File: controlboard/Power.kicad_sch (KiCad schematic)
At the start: 20 parts, among them J11 Pololu Voltage Regulator, J12 USB_C_Receptacle_USB2.0_14P, Q2 PMOS-TODO, U3 AMS1117-3.3, U4 CH224K

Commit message: Control Board major progress
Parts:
- added J15: Jack-DC, symbol Connector:Jack-DC
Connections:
- net GND: now also J15.2
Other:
- note added: "REVERSE PROTECTION"
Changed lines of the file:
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@@
+		)
+	)
+	(text "REVERSE PROTECTION"
+		(exclude_from_sim no)
+		(at 204.724 69.342 0)
+		(effects
+			(font
+				(size 1.27 1.27)
+			)
 		)
 	)
@@
 		)
 	)
+	(hierarchical_label "MotorVoltage"
+		(shape input)
+		(at 207.01 63.5 0)
+		(fields_autoplaced yes)
+		(effects
+			(font
+				(size 1.27 1.27)
+			)
+			(justify left)
+		)
+	)
 	(hierarchical_label "5V"
 		(shape input)
@@
 	(symbol
 		(lib_id "power:GND")
+		(at 191.77 68.58 0)
+		(unit 1)
+		(exclude_from_sim no)
+		(in_bom yes)
+		(on_board yes)
+		(dnp no)
+		(fields_autoplaced yes)
+		(property "Reference" "#PWR09"
+			(at 191.77 74.93 0)
+			(effects
+				(font
+					(size 1.27 1.27)
+				)
+				(hide yes)
+			)
+		)
+		(property "Value" "GND"
+			(at 191.77 73.66 0)
+			(effects
+				(font
+					(size 1.27 1.27)
+				)
+				(hide yes)
+			)
+		)
+		(property "Footprint" ""
+			(at 191.77 68.58 0)
+			(effects
+				(font
+					(size 1.27 1.27)
+				)
+				(hide yes)
+			)
+		)
+		(property "Datasheet" ""
+			(at 191.77 68.58 0)
+			(effects
+				(font
+					(size 1.27 1.27)
+				)
+				(hide yes)
+			)
+		)
+		(property "Description" "Power symbol creates a global label with name \"GND\" , ground"
+			(at 191.77 68.58 0)
+			(effects
+				(font
+					(size 1.27 1.27)
+				)
+				(hide yes)
+			)
+		)
+		(pin "1"
+		)
+		(instances
+			(project "controlboard"
+				(path "/2797250d-6fee-4769-b4dd-0e20ce4f0941/5fab4b81-761e-4fae-b113-00364a75fd9a"
+					(reference "#PWR09")
+					(unit 1)
+				)
+			)
+		)
+	)
+	(symbol
+		(lib_id "power:GND")
 		(at 77.47 43.18 0)
 		(unit 1)
@@
 					(unit 1)
 				)
+			)
+		)
+	)
+	(symbol
+		(lib_id "Connector:Jack-DC")
+		(at 184.15 66.04 0)
+		(unit 1)
+		(exclude_from_sim no)
+		(in_bom yes)
+		(on_board yes)
+		(dnp no)
+		(fields_autoplaced yes)
+		(property "Reference" "J15"
+			(at 184.15 57.15 0)
+			(effects
+				(font
+					(size 1.27 1.27)
+				)
+			)
+		)
+		(property "Value" "Jack-DC"
+			(at 184.15 59.69 0)
+			(effects
+				(font
+					(size 1.27 1.27)
+				)
+			)
+		)
+		(property "Footprint" ""
+			(at 185.42 67.056 0)
+			(effects
+				(font
+					(size 1.27 1.27)
+				)
+				(hide yes)
+			)
+		)
+		(property "Datasheet" "~"
+			(at 185.42 67.056 0)
+			(effects
+				(font
+					(size 1.27 1.27)
+				)
+				(hide yes)
+			)
+		)
+		(property "Description" "DC Barrel Jack"
+			(at 184.15 66.04 0)
+			(effects
+				(font
+					(size 1.27 1.27)
+				)
+				(hide yes)
+			)
+		)
+		(pin "2"
+		)
+		(pin "1"
+		)
+		(instances
+			(project "controlboard"
+				(path "/2797250d-6fee-4769-b4dd-0e20ce4f0941/5fab4b81-761e-4fae-b113-00364a75fd9a"
+					(reference "J15")
+					(unit 1)
+				)

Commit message: more progress on controlboard pcb
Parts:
- removed D2: LED, symbol Device:LED
- removed R2: 1k, symbol Device:R
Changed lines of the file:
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@@
-	)
-	(junction
-		(at 140.97 39.37)
-		(diameter 0)
-		(color 0 0 0 0)
 	)
 	(junction
@@
 	(wire
 		(pts
-			(xy 140.97 39.37) (xy 138.43 39.37)
+			(xy 138.43 39.37) (xy 142.24 39.37)
 		)
 		(stroke
@@
 	(wire
 		(pts
-			(xy 140.97 39.37) (xy 148.59 39.37)
-		)
-		(stroke
-			(width 0)
-			(type default)
-		)
-	)
-	(wire
-		(pts
 			(xy 78.74 49.53) (xy 68.58 49.53)
 		)
@@
 		(pts
 			(xy 113.03 52.07) (xy 120.65 52.07)
-		)
-		(stroke
-			(width 0)
-			(type default)
-		)
-	)
-	(wire
-		(pts
-			(xy 140.97 48.26) (xy 140.97 46.99)
 		)
 		(stroke
@@
 	(hierarchical_label "MotorVoltage"
 		(shape input)
-		(at 148.59 39.37 0)
+		(at 142.24 39.37 0)
 		(fields_autoplaced yes)
 		(effects
@@
 	)
 	(symbol
-		(lib_id "Device:R")
-		(at 140.97 52.07 0)
-		(mirror x)
-		(unit 1)
-		(exclude_from_sim no)
-		(in_bom yes)
-		(on_board yes)
-		(dnp no)
-		(property "Reference" "R2"
-			(at 147.32 52.07 90)
-			(effects
-				(font
-					(size 1.27 1.27)
-				)
-			)
-		)
-		(property "Value" "1k"
-			(at 144.78 52.07 90)
-			(effects
-				(font
-					(size 1.27 1.27)
-				)
-			)
-		)
-		(property "Footprint" ""
-			(at 139.192 52.07 90)
-			(effects
-				(font
-					(size 1.27 1.27)
-				)
-				(hide yes)
-			)
-		)
-		(property "Datasheet" "~"
-			(at 140.97 52.07 0)
-			(effects
-				(font
-					(size 1.27 1.27)
-				)
-				(hide yes)
-			)
-		)
-		(property "Description" "Resistor"
-			(at 140.97 52.07 0)
-			(effects
-				(font
-					(size 1.27 1.27)
-				)
-				(hide yes)
-			)
-		)
-		(pin "2"
-		)
-		(pin "1"
-		)
-		(instances
-			(project "controlboard"
-				(path "/2797250d-6fee-4769-b4dd-0e20ce4f0941/5fab4b81-761e-4fae-b113-00364a75fd9a"
-					(reference "R2")
-					(unit 1)
-				)
-			)
-		)
-	)
-	(symbol
 		(lib_id "Device:C")
 		(at 259.08 92.71 0)
@@
 					(unit 1)
 				)
-			)
-		)
-	)
-	(symbol
-		(lib_id "power:GND")
-		(at 140.97 55.88 0)
-		(unit 1)
-		(exclude_from_sim no)
-		(in_bom yes)
-		(on_board yes)
-		(dnp no)
-		(fields_autoplaced yes)
-		(property "Reference" "#PWR017"
-			(at 140.97 62.23 0)
-			(effects
-				(font
-					(size 1.27 1.27)
-				)
-				(hide yes)
-			)
-		)
-		(property "Value" "GND"
-			(at 140.97 60.96 0)
-			(effects
-				(font
-					(size 1.27 1.27)
-				)
-				(hide yes)
-			)
-		)
-		(property "Footprint" ""
-			(at 140.97 55.88 0)
-			(effects
-				(font
-					(size 1.27 1.27)
-				)
-				(hide yes)
-			)
-		)
-		(property "Datasheet" ""
-			(at 140.97 55.88 0)
-			(effects
-				(font
-					(size 1.27 1.27)
-				)
-				(hide yes)
-			)
-		)
-		(property "Description" "Power symbol creates a global label with name \"GND\" , ground"
-			(at 140.97 55.88 0)
-			(effects
-				(font
-					(size 1.27 1.27)
-				)
-				(hide yes)
-			)
-		)
-		(pin "1"
-		)
-		(instances
-			(project "controlboard"
-				(path "/2797250d-6fee-4769-b4dd-0e20ce4f0941/5fab4b81-761e-4fae-b113-00364a75fd9a"
-					(reference "#PWR017")
-					(unit 1)
-				)
-			)
-		)
-	)
-	(symbol
-		(lib_id "Device:LED")
-		(at 140.97 43.18 270)
-		(mirror x)
-		(unit 1)
-		(exclude_from_sim no)
-		(in_bom yes)
-		(on_board yes)
-		(dnp no)
-		(property "Reference" "D2"
-			(at 147.32 44.7675 0)
-			(effects
-				(font
-					(size 1.27 1.27)
-				)
-			)
-		)
-		(property "Value" "LED"
-			(at 144.78 44.7675 0)
-			(effects
-				(font
-					(size 1.27 1.27)
-				)
-			)
-		)
-		(property "Footprint" ""
-			(at 140.97 43.18 0)
-			(effects
-				(font
-					(size 1.27 1.27)
-				)
-				(hide yes)
-			)
-		)
-		(property "Datasheet" "~"
-			(at 140.97 43.18 0)
-			(effects
-				(font
-					(size 1.27 1.27)
-				)
-				(hide yes)
-			)
-		)
-		(property "Description" "Light emitting diode"
-			(at 140.97 43.18 0)
-			(effects
-				(font
-					(size 1.27 1.27)
-				)
-				(hide yes)
-			)
-		)
-		(pin "1"
-		)
-		(pin "2"
-		)
-		(instances
-			(project "controlboard"
-				(path "/2797250d-6fee-4769-b4dd-0e20ce4f0941/5fab4b81-761e-4fae-b113-00364a75fd9a"
-					(reference "D2")
-					(unit 1)
-				)

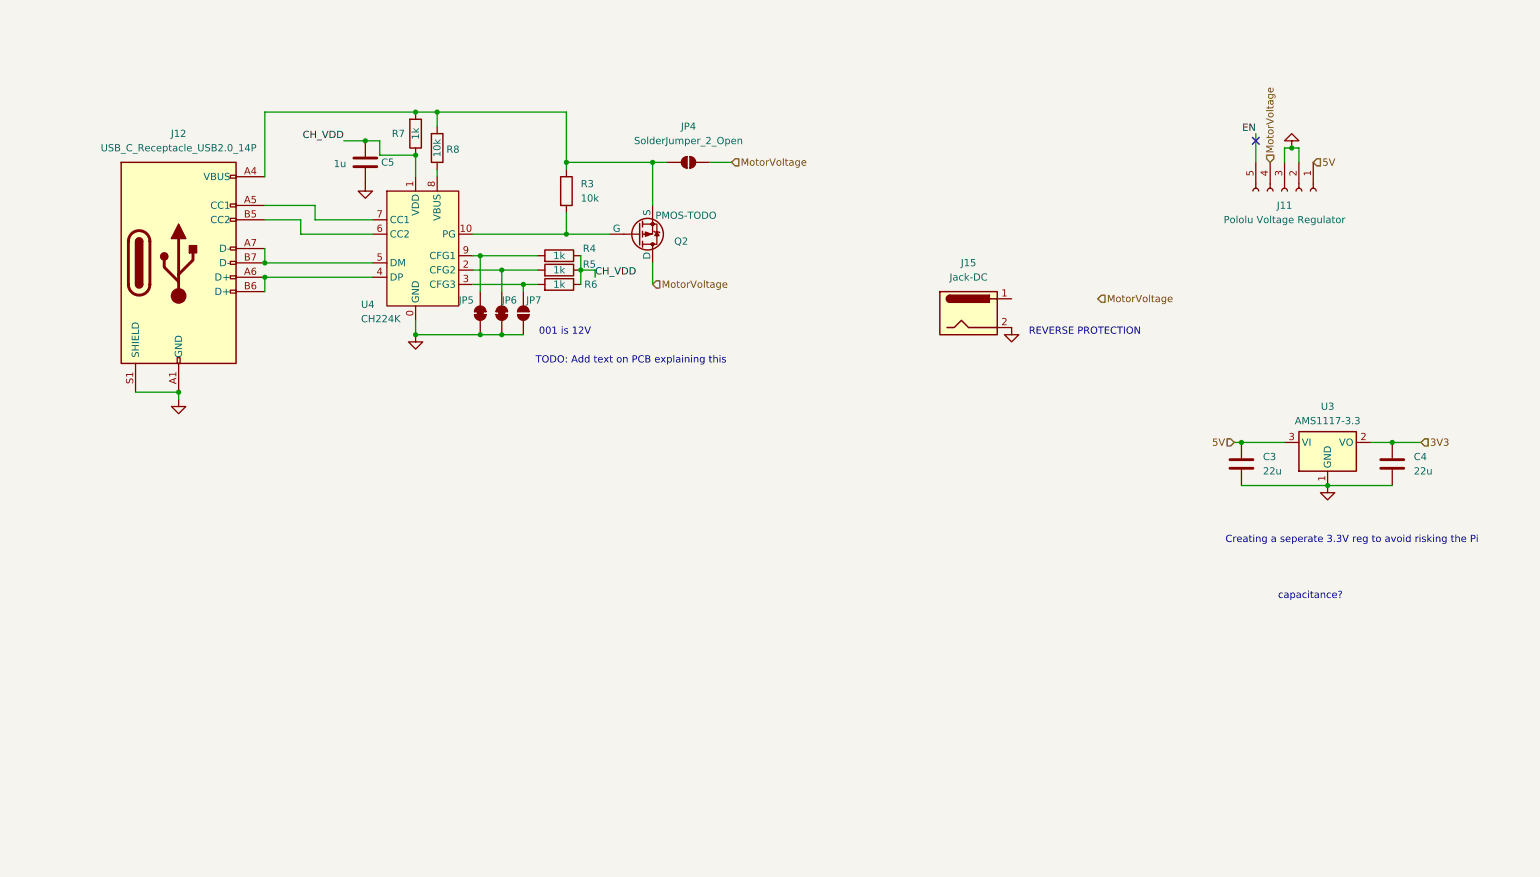
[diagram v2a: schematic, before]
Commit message: ControlBoard Schematic nearly done
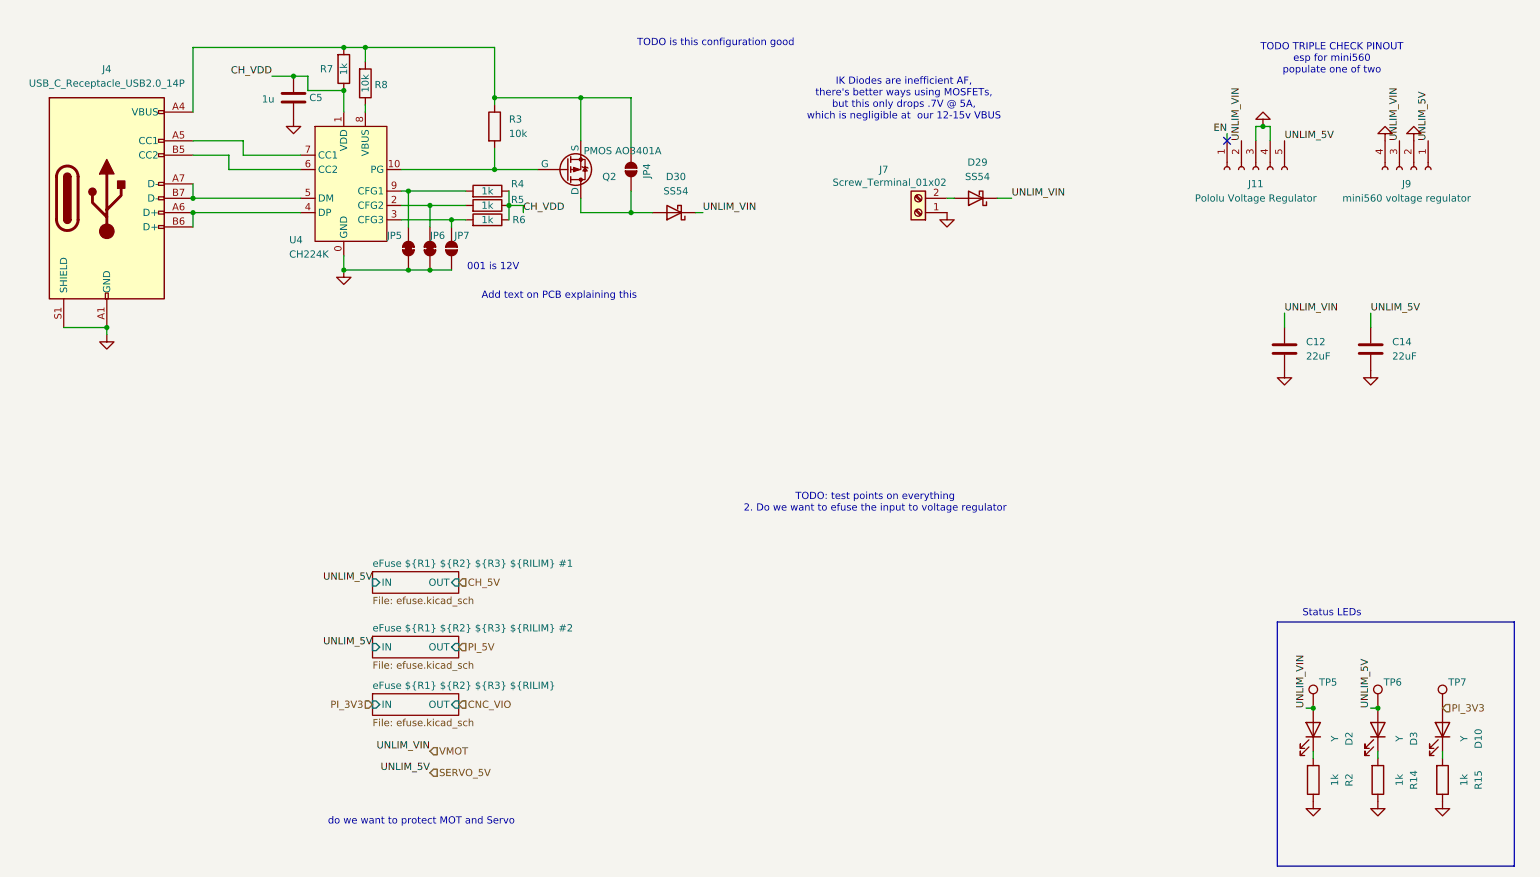
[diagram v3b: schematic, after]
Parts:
- removed C3, C4: 22u, symbol Device:C
- removed J15: Jack-DC, symbol Connector:Jack-DC
- removed U3: AMS1117-3.3, Package_TO_SOT_SMD:SOT-223-3_TabPin2, symbol Regulator_Linear:AMS1117-3.3
- added C12, C14: 22uF, Capacitor_SMD:C_1206_3216Metric_Pad1.33x1.80mm_HandSolder, symbol Device:C
- added D10, D2, D3: Y, LED_SMD:LED_0603_1608Metric_Pad1.05x0.95mm_HandSolder, symbol Device:LED
- added D29, D30: SS54, Diode_SMD:D_SMA_Handsoldering, symbol Device:D_Schottky
- added J7: Screw_Terminal_01x02, TerminalBlock_RND:TerminalBlock_RND_205-00287_1x02_P5.08mm_Horizontal, symbol Connector:Screw_Terminal_01x02
- added J9: mini560 voltage regulator, 0chessbot-parts:mini560, symbol Connector:Conn_01x04_Socket
- added R14, R15, R2: 1k, Resistor_SMD:R_0603_1608Metric_Pad0.98x0.95mm_HandSolder, symbol Device:R
- added TP5, TP6, TP7: TestPoint, Connector_PinSocket_2.54mm:PinSocket_1x01_P2.54mm_Vertical, symbol Connector:TestPoint
- C5: footprint (none) -> Capacitor_SMD:C_0603_1608Metric_Pad1.08x0.95mm_HandSolder
- J11: footprint (none) -> 0chessbot-parts:reg15d
- J4: renamed from J12; footprint (none) -> Connector_USB:USB_C_Receptacle_HRO_TYPE-C-31-M-12
- JP4, JP7: footprint (none) -> Jumper:SolderJumper-2_P1.3mm_Open_RoundedPad1.0x1.5mm
- JP5, JP6: footprint (none) -> Jumper:SolderJumper-2_P1.3mm_Bridged2Bar_RoundedPad1.0x1.5mm
- Q2: value PMOS-TODO -> PMOS AO3401A; footprint (none) -> Package_TO_SOT_SMD:SOT-23_Handsoldering
- R3, R4, R5, R6, R7, R8: footprint (none) -> Resistor_SMD:R_0603_1608Metric_Pad0.98x0.95mm_HandSolder
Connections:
- net 5V is gone; now on net EN: J11.1 (Pin_1)
- net EN: no longer J11.5 (Pin_5)
- net GND: now also J11.4 (Pin_4), C12.2, C14.2, J7.1 (Pin_1), J9.2 (Pin_2), J9.4 (Pin_4), R14.1, R15.1, R2.1; no longer J11.2 (Pin_2)
- net MotorVoltage: no longer names the net of JP4.2 (B), Q2.1 (D)
- net MotorVoltage: now also D30.2 (A); no longer J11.4 (Pin_4)
- new net: D10.1 (K), R15.2
- new net: D29.2 (A), J7.2 (Pin_2)
- new net: D3.1 (K), R14.2
- new net: D2.1 (K), R2.2
- new net PI_3V3: D10.2 (A), TP7.1
- new net SERVO_5V: C14.1, D3.2 (A), J11.5 (Pin_5), J9.1 (Pin_1), TP6.1
- new net VMOT: C12.1, D2.2 (A), D29.1 (K), D30.1 (K), J11.2 (Pin_2), J9.3 (Pin_3), TP5.1
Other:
- added sheet eFuse ${R1} ${R2} ${R3} ${RILIM} (efuse.kicad_sch)
- added sheet eFuse ${R1} ${R2} ${R3} ${RILIM} #1 (efuse.kicad_sch)
- added sheet eFuse ${R1} ${R2} ${R3} ${RILIM} #2 (efuse.kicad_sch)
- note added: "Add text on PCB explaining this"
- note added: "IK Diodes are inefficient AF, there's better ways using MOSFETs, but this only drops .7V @ 5A, which is negligible at our 12-15v VBUS"
- note added: "Status LEDs"
- note added: "TODO TRIPLE CHECK PINOUT esp for mini560 populate one of two"
- note added: "TODO is this configuration good"
- note added: "TODO: test points on everything 2. Do we want to efuse the input to voltage regulator"
- note added: "do we want to protect MOT and Servo"
- note removed: "Creating a seperate 3.3V reg to avoid risking the Pi"
- note removed: "REVERSE PROTECTION"
- note removed: "TODO: Add text on PCB explaining this"
- note removed: "capacitance?"
- moved on the sheet: C5, J11, J4, JP5, JP6, JP7, Q2, R3, R4, R5, R6, R7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

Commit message: schematic improvements
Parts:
- added JP25: SolderJumper_2_Bridged, symbol Jumper:SolderJumper_2_Bridged
- added SW3: Main Power Switch/EStop, Connector_PinSocket_2.54mm:PinSocket_1x02_P2.54mm_Vertical, symbol Switch:SW_Push
- added TP11, TP12, TP13, TP14: TestPoint, symbol Connector:TestPoint
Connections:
- net CH_VDD: now also TP14.1
- net at J4.A4 (VBUS), J4.A9 (VBUS), J4.B4 (VBUS)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: now also TP11.1
- net at J4.A5 (CC1), U4.7 (CC1): now also TP12.1
- net at J4.B5 (CC2), U4.6 (CC2): now also TP13.1
- net at Q2.2 (G), R3.2: now also JP25.2 (B), SW3.2; no longer U4.10 (PG)
- net EN: no longer names the net of J11.1 (Pin_1)
- net SERVO_5V renamed UNLIM_5V
- new net: JP25.1 (A), SW3.1, U4.10 (PG)
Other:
- note added: "Chessboard and servo get the same protected line"
- note added: "Future thought: do we want to protect VMOT (emag/steppers)"
- note added: "TODO TRIPLE CHECK PINOUT esp for mini560 (from amazon) populate one of two"
- note added: "TODO: Do we want to efuse the input to voltage regulator"
- note added: "bypass till we buy a switch"
- note removed: "TODO TRIPLE CHECK PINOUT esp for mini560 populate one of two"
- note removed: "TODO is this configuration good"
- note removed: "TODO: test points on everything 2. Do we want to efuse the input to voltage regulator"
- note removed: "do we want to protect MOT and Servo"
- moved on the sheet: R3

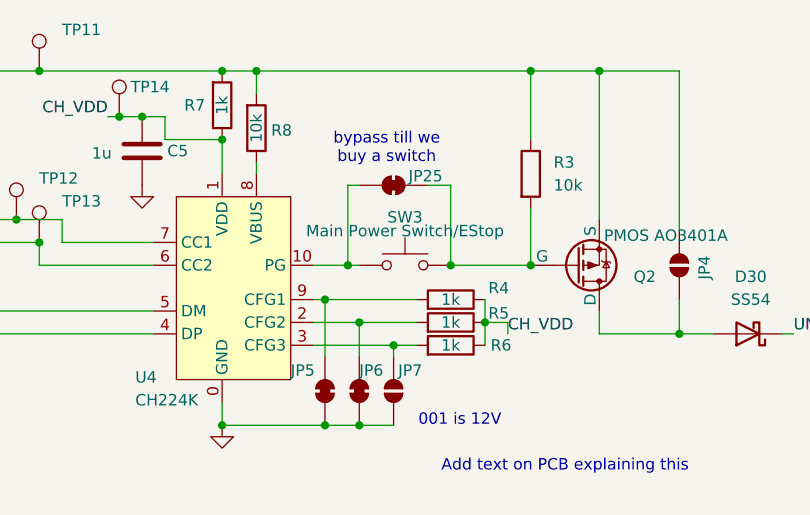
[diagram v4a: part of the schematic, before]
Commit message: improve pinout
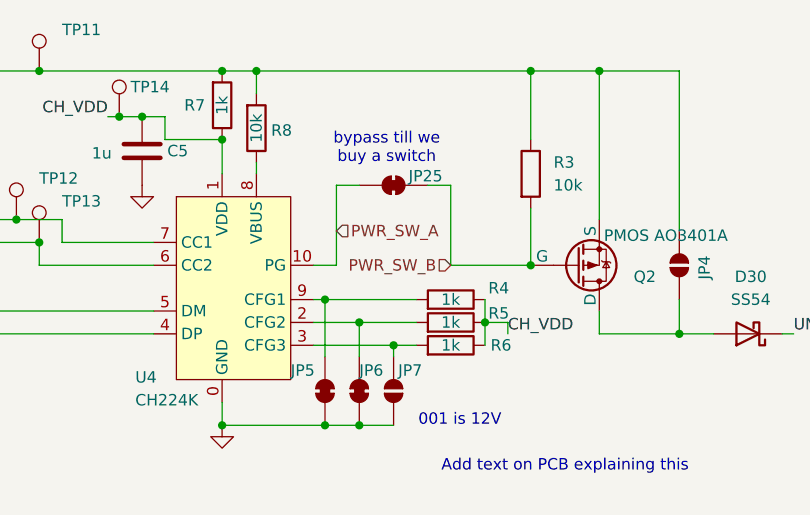
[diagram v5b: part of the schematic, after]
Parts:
- removed SW3: Main Power Switch/EStop, Connector_PinSocket_2.54mm:PinSocket_1x02_P2.54mm_Vertical, symbol Switch:SW_Push
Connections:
- net PWR_SW_A: now reaches JP25.1 (A), U4.10 (PG)
- net PWR_SW_B: now reaches JP25.2 (B), Q2.2 (G), R3.2
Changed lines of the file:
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@@
-	)
-	(junction
-		(at 87.63 40.64)
-		(diameter 0)
-		(color 0 0 0 0)
 	)
 	(junction
@@
 	(junction
 		(at 73.66 19.05)
-		(diameter 0)
-		(color 0 0 0 0)
-	)
-	(junction
-		(at 99.06 40.64)
 		(diameter 0)
 		(color 0 0 0 0)
@@
 	(wire
 		(pts
+			(xy 86.36 40.64) (xy 83.82 40.64)
+		)
+		(stroke
+			(width 0)
+			(type default)
+		)
+	)
+	(wire
+		(pts
 			(xy 73.66 58.42) (xy 73.66 55.88)
 		)
@@
 	(wire
 		(pts
-			(xy 88.9 31.75) (xy 87.63 31.75)
+			(xy 88.9 31.75) (xy 86.36 31.75)
 		)
 		(stroke
@@
 	(wire
 		(pts
-			(xy 87.63 31.75) (xy 87.63 40.64)
+			(xy 86.36 31.75) (xy 86.36 40.64)
 		)
 		(stroke
@@
 		(pts
 			(xy 88.9 58.42) (xy 92.71 58.42)
-		)
-		(stroke
-			(width 0)
-			(type default)
-		)
-	)
-	(wire
-		(pts
-			(xy 87.63 40.64) (xy 88.9 40.64)
-		)
-		(stroke
-			(width 0)
-			(type default)
-		)
-	)
-	(wire
-		(pts
-			(xy 83.82 40.64) (xy 87.63 40.64)
 		)
 		(stroke
@@
 		)
 	)
+	(hierarchical_label "PWR_SW_A"
+		(shape input)
+		(at 86.36 36.83 0)
+		(fields_autoplaced yes)
+		(effects
+			(font
+				(size 1.27 1.27)
+			)
+			(justify left)
+		)
+	)
 	(hierarchical_label "SERVO_5V"
 		(shape input)
@@
 			)
 			(justify left)
+		)
+	)
+	(hierarchical_label "PWR_SW_B"
+		(shape input)
+		(at 99.06 40.64 180)
+		(fields_autoplaced yes)
+		(effects
+			(font
+				(size 1.27 1.27)
+			)
+			(justify right)
 		)
 	)
@@
 					(unit 1)
 				)
-			)
-		)
-	)
-	(symbol
-		(lib_id "Switch:SW_Push")
-		(at 93.98 40.64 0)
-		(unit 1)
-		(exclude_from_sim no)
-		(in_bom yes)
-		(on_board yes)
-		(dnp no)
-		(property "Reference" "SW3"
-			(at 93.98 35.306 0)
-			(effects
-				(font
-					(size 1.27 1.27)
-				)
-			)
-		)
-		(property "Value" "Main Power Switch/EStop"
-			(at 93.98 36.83 0)
-			(effects
-				(font
-					(size 1.27 1.27)
-				)
-			)
-		)
-		(property "Footprint" "Connector_PinSocket_2.54mm:PinSocket_1x02_P2.54mm_Vertical"
-			(at 93.98 35.56 0)
-			(effects
-				(font
-					(size 1.27 1.27)
-				)
-				(hide yes)
-			)
-		)
-		(property "Datasheet" "~"
-			(at 93.98 35.56 0)
-			(effects
-				(font
-					(size 1.27 1.27)
-				)
-				(hide yes)
-			)
-		)
-		(property "Description" "Push button switch, generic, two pins"
-			(at 93.98 40.64 0)
-			(effects
-				(font
-					(size 1.27 1.27)
-				)
-				(hide yes)
-			)
-		)
-		(pin "2"
-		)
-		(pin "1"
-		)
-		(instances
-			(project "controlboard"
-				(path "/2797250d-6fee-4769-b4dd-0e20ce4f0941/5fab4b81-761e-4fae-b113-00364a75fd9a"
-					(reference "SW3")
-					(unit 1)
-				)

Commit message: improvements
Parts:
- JP25: footprint (none) -> Jumper:SolderJumper-2_P1.3mm_Bridged2Bar_RoundedPad1.0x1.5mm
- TP11, TP12, TP13, TP14: footprint (none) -> Connector_PinSocket_2.54mm:PinSocket_1x01_P2.54mm_Vertical
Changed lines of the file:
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@@
 			)
 		)
-		(property "Footprint" ""
+		(property "Footprint" "Jumper:SolderJumper-2_P1.3mm_Bridged2Bar_RoundedPad1.0x1.5mm"
 			(at 92.71 31.75 0)
 			(effects
@@
 			)
 		)
-		(property "Footprint" ""
+		(property "Footprint" "Connector_PinSocket_2.54mm:PinSocket_1x01_P2.54mm_Vertical"
 			(at 67.31 24.13 0)
 			(effects
@@
 			)
 		)
-		(property "Footprint" ""
+		(property "Footprint" "Connector_PinSocket_2.54mm:PinSocket_1x01_P2.54mm_Vertical"
 			(at 58.42 38.1 0)
 			(effects
@@
 			)
 		)
-		(property "Footprint" ""
+		(property "Footprint" "Connector_PinSocket_2.54mm:PinSocket_1x01_P2.54mm_Vertical"
 			(at 58.42 19.05 0)
 			(effects
@@
 			)
 		)
-		(property "Footprint" ""
+		(property "Footprint" "Connector_PinSocket_2.54mm:PinSocket_1x01_P2.54mm_Vertical"
 			(at 55.88 35.56 0)
 			(effects
